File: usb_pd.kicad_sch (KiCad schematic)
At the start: 81 parts, among them Q1 Q_NMOS_DGS, Q2 Q_NMOS_DGS, Q3 Q_NMOS_DGS, Q4 Q_NMOS_DGS, U5 TPS5403DR, U6 MP28167GQ-P, U7 BQ25731

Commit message: added nfc antenna components, added most of footprints
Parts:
- C14, C30: footprint Capacitor_SMD:C_0805_2012Metric_Pad1.18x1.45mm_HandSolder -> (none)
- C15, C25, C27, C28, C29, C31, C32, C33, C34, C35, C36, C37, C38, C39, C40, C49, C50, C57, C58, C59, C60, C61, C62: footprint (none) -> Capacitor_SMD:C_0603_1608Metric_Pad1.08x0.95mm_HandSolder
- L1: footprint smarthome:Inductor_104CDMCC -> airsoft_controller:Inductor_104CDMCC
- R11, R12, R13, R14, R15, R16, R17, R18, R19, R20, R22, R23, R24, R5, R7, R8, R9: footprint (none) -> Resistor_SMD:R_0603_1608Metric_Pad0.98x0.95mm_HandSolder
- U6: footprint (none) -> airsoft_controller:QFN-16

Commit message: schematic creation
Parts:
- removed Q1, Q2, Q3, Q4: Q_NMOS_DGS, symbol Device:Q_NMOS_DGS
- added C57, C60: 10uF MLCC 25V, Capacitor_SMD:C_0805_2012Metric_Pad1.18x1.45mm_HandSolder, symbol Device:C
- added Q1, Q2: Q_Dual_NMOS, airsoft_controller:Q_DUAL_NMOS_DMT3006LPB, symbol airsoft_controller:Q_Dual_NMOS_G1D1D1D1S2S2S2G2S1
- C14, C44, C45: footprint (none) -> Capacitor_SMD:C_0805_2012Metric_Pad1.18x1.45mm_HandSolder
- C16: renamed from C17; footprint (none) -> Capacitor_SMD:CP_Elec_6.3x5.4; symbol Device:C -> Device:C_Polarized
- C18, C19, C20, C21, C22, C23, C51, C52, C53, C54, C55, C56: value 10uF -> 10uF MLCC 25V; footprint (none) -> Capacitor_SMD:C_0805_2012Metric_Pad1.18x1.45mm_HandSolder
- C30: footprint (none) -> Capacitor_SMD:C_1206_3216Metric_Pad1.33x1.80mm_HandSolder
- C41, C43: footprint (none) -> Capacitor_SMD:CP_Elec_6.3x7.7; symbol Device:C -> Device:C_Polarized
- C42: footprint (none) -> Capacitor_SMD:CP_Elec_5x5.3; symbol Device:C -> Device:C_Polarized
- C46, C47: value 33uF -> 22uF POSCAP 25V; footprint (none) -> Capacitor_SMD:C_1210_3225Metric_Pad1.33x2.70mm_HandSolder; symbol Device:C -> Device:C_Polarized
- C48: value 10uF -> 10uF MLCC 25V; footprint (none) -> Capacitor_SMD:C_1206_3216Metric_Pad1.33x1.80mm_HandSolder
- L2: footprint (none) -> airsoft_controller:Inductor_SRP1265C
- L3: footprint (none) -> airsoft_controller:Inductor_WLPMA0A040
- R21: footprint (none) -> Resistor_SMD:R_0612_1632Metric_Pad1.18x3.40mm_HandSolder
- R8: renamed from R10; footprint (none) -> Resistor_SMD:R_0612_1632Metric_Pad1.18x3.40mm_HandSolder
- renumbered C16 to C17, C29 to C28, C28 to C29, C57 to C63, C60 to C64, R12 to R10, R13 to R11, R14 to R12, R15 to R13, R16 to R14, R17 to R15, R18 to R16, R19 to R17, R22 to R18, R23 to R19, R5 to R2, R24 to R22, R4 to R3, R6 to R4, R7 to R5, R8 to R6, R9 to R7, R11 to R9
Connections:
- net BQ_VSYS: now also C46.1, C47.1, C57.2, C60.2, Q2.2 (D1), Q2.3 (D1), Q2.4 (D1); no longer C46.2, C47.2
- net GND: now also C16.2, C25.2, C46.2, C47.2, C57.1, C60.1, Q1.5 (S2), Q1.6 (S2), Q1.7 (S2), Q2.5 (S2), Q2.6 (S2), Q2.7 (S2); no longer C16.1, C25.1, C46.1, C47.1
- net SYS VBUS: now also C16.1; no longer C16.2
- net at C31.2, C32.2, R8.2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: now also Q1.2 (D1), Q1.3 (D1), Q1.4 (D1)
- net at C35.2, L2.1, U7.32 (SW1): now also Q1.9 (S1/D2), Q1.9 (S1/D2)
- net at C40.2, L2.2, U7.23 (SW2): now also Q2.9 (S1/D2), Q2.9 (S1/D2)
- net at C27.1, R6.2, U7.3 (ACP): now also C25.1; no longer C25.2
- net at U7.31 (HIDRV1): now also Q1.1 (G1)
- net at U7.29 (LODRV1): now also Q1.8 (G2)
- net at U7.26 (LODRV2): now also Q2.8 (G2)
- net at U7.24 (HIDRV2): now also Q2.1 (G1)
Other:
- note added: "10nF - 400kHz open - 800kHz"
- note added: "65W - 7*10uF >90W - 9*10uF"
- note added: "Optional"
- moved on the sheet: C14, C15, C25, C27, C29, C63, C64, R2, R20, R21, R22

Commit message: edited usb pcb part
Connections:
- net +3V3 is gone; now on net +3.3V: R15.1
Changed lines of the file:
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@@
     (pin "2")
   )
-  (symbol (lib_id "power:+3V3") (at 180.34 113.03 0) (unit 1)
+  (symbol (lib_id "power:+3.3V") (at 180.34 113.03 0) (unit 1)
     (in_bom yes) (on_board yes) (fields_autoplaced)
     (property "Reference" "#PWR065" (id 0) (at 180.34 116.84 0)

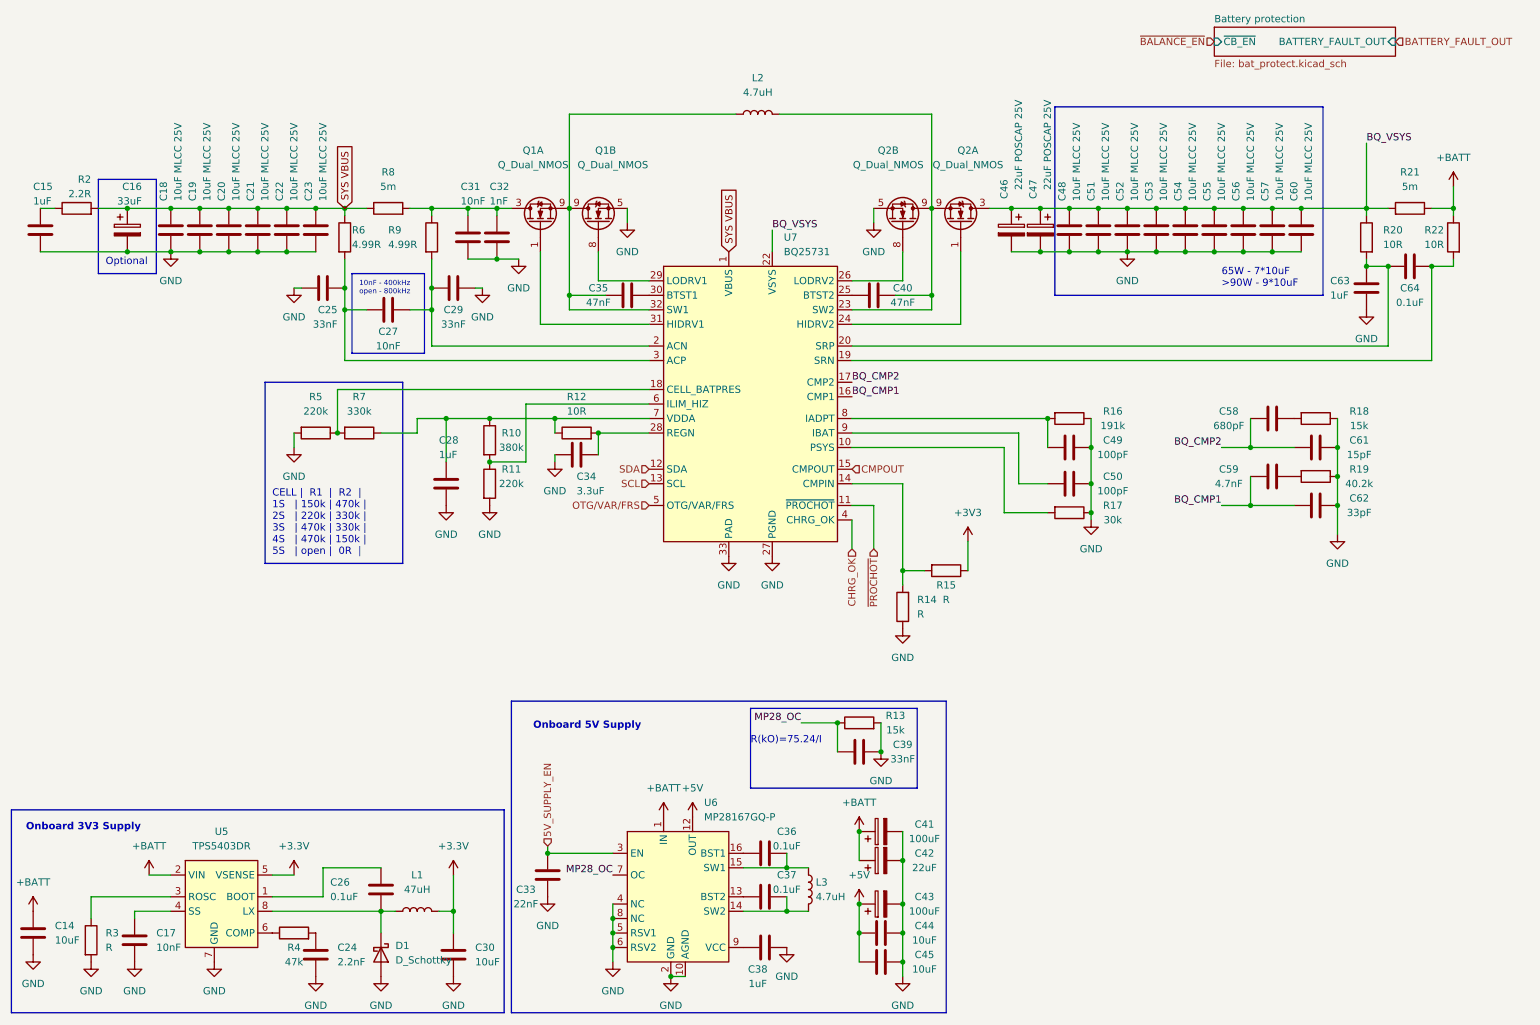
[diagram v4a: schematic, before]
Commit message: done first iteration of pcb routing, slikscreen still broken
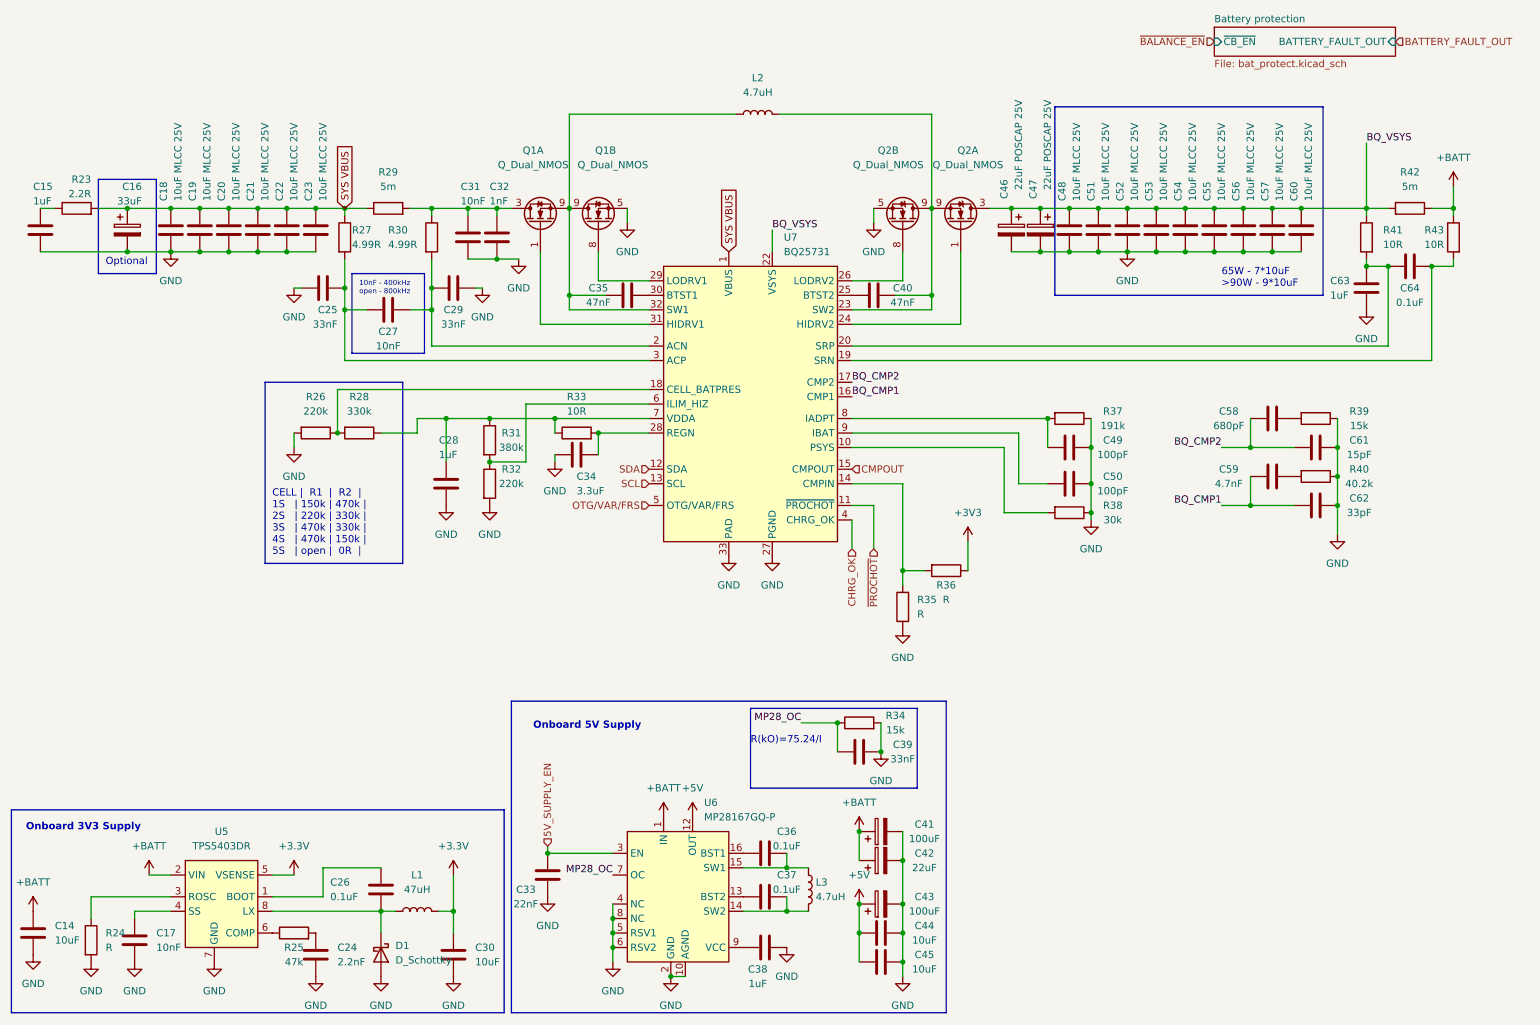
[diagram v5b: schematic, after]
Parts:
- C30, C48: footprint Capacitor_SMD:C_1206_3216Metric_Pad1.33x1.80mm_HandSolder -> Capacitor_SMD:C_0805_2012Metric_Pad1.18x1.45mm_HandSolder
- renumbered R2 to R23, R3 to R24, R4 to R25, R5 to R26, R6 to R27, R7 to R28, R8 to R29, R9 to R30, R10 to R31, R11 to R32, R12 to R33, R13 to R34, R14 to R35, R15 to R36, R16 to R37, R17 to R38, R18 to R39, R19 to R40, R20 to R41, R21 to R42, R22 to R43

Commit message: mounting holes, fixes silkscreen
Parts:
- renumbered R23 to R22, R24 to R23, R25 to R24, R26 to R25, R27 to R26, R28 to R27, R29 to R28, R30 to R29, R31 to R30, R32 to R31, R33 to R32, R34 to R33, R35 to R34, R36 to R35, R37 to R36, R38 to R37, R39 to R38, R40 to R39, R41 to R40, R42 to R41, R43 to R42
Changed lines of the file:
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@@
   (symbol (lib_id "Device:R") (at 86.36 59.69 0) (unit 1)
     (in_bom yes) (on_board yes)
-    (property "Reference" "R30" (id 0) (at 78.74 58.42 0)
+    (property "Reference" "R29" (id 0) (at 78.74 58.42 0)
       (effects (font (size 1.27 1.27)) (justify left))
     )
@@
   (symbol (lib_id "Device:R") (at 96.52 102.87 0) (unit 1)
     (in_bom yes) (on_board yes)
-    (property "Reference" "R32" (id 0) (at 100.33 100.33 0))
+    (property "Reference" "R31" (id 0) (at 100.33 100.33 0))
     (property "Value" "220k" (id 1) (at 100.33 102.87 0))
     (property "Footprint" "Resistor_SMD:R_0603_1608Metric_Pad0.98x0.95mm_HandSolder" (id 2) (at 94.742 102.87 90)
@@
   (symbol (lib_id "Device:R") (at 71.12 59.69 0) (unit 1)
     (in_bom yes) (on_board yes)
-    (property "Reference" "R27" (id 0) (at 72.39 58.42 0)
+    (property "Reference" "R26" (id 0) (at 72.39 58.42 0)
       (effects (font (size 1.27 1.27)) (justify left))
     )
@@
   (symbol (lib_id "Device:R") (at 176.53 118.11 270) (unit 1)
     (in_bom yes) (on_board yes)
-    (property "Reference" "R36" (id 0) (at 176.53 120.65 90))
+    (property "Reference" "R35" (id 0) (at 176.53 120.65 90))
     (property "Value" "R" (id 1) (at 176.53 123.19 90))
     (property "Footprint" "Resistor_SMD:R_0603_1608Metric_Pad0.98x0.95mm_HandSolder" (id 2) (at 176.53 116.332 90)
@@
   (symbol (lib_id "Device:R") (at 265.43 59.69 0) (mirror y) (unit 1)
     (in_bom yes) (on_board yes)
-    (property "Reference" "R43" (id 0) (at 260.35 58.42 0)
+    (property "Reference" "R42" (id 0) (at 260.35 58.42 0)
       (effects (font (size 1.27 1.27)) (justify right))
     )
@@
   (symbol (lib_id "Device:R") (at 78.74 54.61 90) (unit 1)
     (in_bom yes) (on_board yes) (fields_autoplaced)
-    (property "Reference" "R29" (id 0) (at 78.74 48.26 90))
+    (property "Reference" "R28" (id 0) (at 78.74 48.26 90))
     (property "Value" "5m" (id 1) (at 78.74 50.8 90))
     (property "Footprint" "Resistor_SMD:R_0612_1632Metric_Pad1.18x3.40mm_HandSolder" (id 2) (at 78.74 56.388 90)
@@
   (symbol (lib_id "Device:R") (at 62.23 181.61 90) (unit 1)
     (in_bom yes) (on_board yes)
-    (property "Reference" "R25" (id 0) (at 62.23 184.15 90))
+    (property "Reference" "R24" (id 0) (at 62.23 184.15 90))
     (property "Value" "47k" (id 1) (at 62.23 186.69 90))
     (property "Footprint" "Resistor_SMD:R_0603_1608Metric_Pad0.98x0.95mm_HandSolder" (id 2) (at 62.23 183.388 90)
@@
   (symbol (lib_id "Device:R") (at 168.91 124.46 180) (unit 1)
     (in_bom yes) (on_board yes) (fields_autoplaced)
-    (property "Reference" "R35" (id 0) (at 171.45 123.1899 0)
+    (property "Reference" "R34" (id 0) (at 171.45 123.1899 0)
       (effects (font (size 1.27 1.27)) (justify right))
     )
@@
   (symbol (lib_id "Device:R") (at 24.13 54.61 90) (unit 1)
     (in_bom yes) (on_board yes)
-    (property "Reference" "R23" (id 0) (at 26.67 49.53 90)
+    (property "Reference" "R22" (id 0) (at 26.67 49.53 90)
       (effects (font (size 1.27 1.27)) (justify left))
     )
@@
   (symbol (lib_id "Device:R") (at 250.19 59.69 0) (mirror y) (unit 1)
     (in_bom yes) (on_board yes)
-    (property "Reference" "R41" (id 0) (at 256.54 58.42 0)
+    (property "Reference" "R40" (id 0) (at 256.54 58.42 0)
       (effects (font (size 1.27 1.27)) (justify left))
     )
@@
   (symbol (lib_id "Device:R") (at 111.76 93.98 90) (unit 1)
     (in_bom yes) (on_board yes) (fields_autoplaced)
-    (property "Reference" "R33" (id 0) (at 111.76 87.63 90))
+    (property "Reference" "R32" (id 0) (at 111.76 87.63 90))
     (property "Value" "10R" (id 1) (at 111.76 90.17 90))
     (property "Footprint" "Resistor_SMD:R_0603_1608Metric_Pad0.98x0.95mm_HandSolder" (id 2) (at 111.76 95.758 90)
@@
   (symbol (lib_id "Device:R") (at 73.66 93.98 270) (unit 1)
     (in_bom yes) (on_board yes) (fields_autoplaced)
-    (property "Reference" "R28" (id 0) (at 73.66 87.63 90))
+    (property "Reference" "R27" (id 0) (at 73.66 87.63 90))
     (property "Value" "330k" (id 1) (at 73.66 90.17 90))
     (property "Footprint" "Resistor_SMD:R_0603_1608Metric_Pad0.98x0.95mm_HandSolder" (id 2) (at 73.66 92.202 90)
@@
   (symbol (lib_id "Device:R") (at 198.12 107.95 270) (unit 1)
     (in_bom yes) (on_board yes)
-    (property "Reference" "R38" (id 0) (at 205.74 106.68 90))
+    (property "Reference" "R37" (id 0) (at 205.74 106.68 90))
     (property "Value" "30k" (id 1) (at 205.74 109.22 90))
     (property "Footprint" "Resistor_SMD:R_0603_1608Metric_Pad0.98x0.95mm_HandSolder" (id 2) (at 198.12 106.172 90)
@@
   (symbol (lib_id "Device:R") (at 161.29 144.78 90) (unit 1)
     (in_bom yes) (on_board yes)
-    (property "Reference" "R34" (id 0) (at 167.64 143.51 90))
+    (property "Reference" "R33" (id 0) (at 167.64 143.51 90))
     (property "Value" "15k" (id 1) (at 167.64 146.05 90))
     (property "Footprint" "Resistor_SMD:R_0603_1608Metric_Pad0.98x0.95mm_HandSolder" (id 2) (at 161.29 146.558 90)
@@
   (symbol (lib_id "Device:R") (at 257.81 54.61 270) (mirror x) (unit 1)
     (in_bom yes) (on_board yes) (fields_autoplaced)
-    (property "Reference" "R42" (id 0) (at 257.81 48.26 90))
+    (property "Reference" "R41" (id 0) (at 257.81 48.26 90))
     (property "Value" "5m" (id 1) (at 257.81 50.8 90))
     (property "Footprint" "Resistor_SMD:R_0612_1632Metric_Pad1.18x3.40mm_HandSolder" (id 2) (at 257.81 56.388 90)
@@
   (symbol (lib_id "Device:R") (at 26.67 182.88 0) (unit 1)
     (in_bom yes) (on_board yes) (fields_autoplaced)
-    (property "Reference" "R24" (id 0) (at 29.21 181.6099 0)
+    (property "Reference" "R23" (id 0) (at 29.21 181.6099 0)
       (effects (font (size 1.27 1.27)) (justify left))
     )
@@
   (symbol (lib_id "Device:R") (at 241.3 101.6 270) (unit 1)
     (in_bom yes) (on_board yes)
-    (property "Reference" "R40" (id 0) (at 248.92 100.33 90))
+    (property "Reference" "R39" (id 0) (at 248.92 100.33 90))
     (property "Value" "40.2k" (id 1) (at 248.92 102.87 90))
     (property "Footprint" "Resistor_SMD:R_0603_1608Metric_Pad0.98x0.95mm_HandSolder" (id 2) (at 241.3 99.822 90)
@@
   (symbol (lib_id "Device:R") (at 241.3 91.44 270) (unit 1)
     (in_bom yes) (on_board yes)
-    (property "Reference" "R39" (id 0) (at 248.92 90.17 90))
+    (property "Reference" "R38" (id 0) (at 248.92 90.17 90))
     (property "Value" "15k" (id 1) (at 248.92 92.71 90))
     (property "Footprint" "Resistor_SMD:R_0603_1608Metric_Pad0.98x0.95mm_HandSolder" (id 2) (at 241.3 89.662 90)
@@
   (symbol (lib_id "Device:R") (at 66.04 93.98 270) (unit 1)
     (in_bom yes) (on_board yes) (fields_autoplaced)
-    (property "Reference" "R26" (id 0) (at 66.04 87.63 90))
+    (property "Reference" "R25" (id 0) (at 66.04 87.63 90))
     (property "Value" "220k" (id 1) (at 66.04 90.17 90))
     (property "Footprint" "Resistor_SMD:R_0603_1608Metric_Pad0.98x0.95mm_HandSolder" (id 2) (at 66.04 92.202 90)
@@
   (symbol (lib_id "Device:R") (at 198.12 91.44 270) (unit 1)
     (in_bom yes) (on_board yes)
-    (property "Reference" "R37" (id 0) (at 205.74 90.17 90))
+    (property "Reference" "R36" (id 0) (at 205.74 90.17 90))
     (property "Value" "191k" (id 1) (at 205.74 92.71 90))
     (property "Footprint" "Resistor_SMD:R_0603_1608Metric_Pad0.98x0.95mm_HandSolder" (id 2) (at 198.12 89.662 90)
@@
   (symbol (lib_id "Device:R") (at 96.52 95.25 0) (unit 1)
     (in_bom yes) (on_board yes)
-    (property "Reference" "R31" (id 0) (at 100.33 93.98 0))
+    (property "Reference" "R30" (id 0) (at 100.33 93.98 0))
     (property "Value" "380k" (id 1) (at 100.33 96.52 0))
     (property "Footprint" "Resistor_SMD:R_0603_1608Metric_Pad0.98x0.95mm_HandSolder" (id 2) (at 94.742 95.25 90)

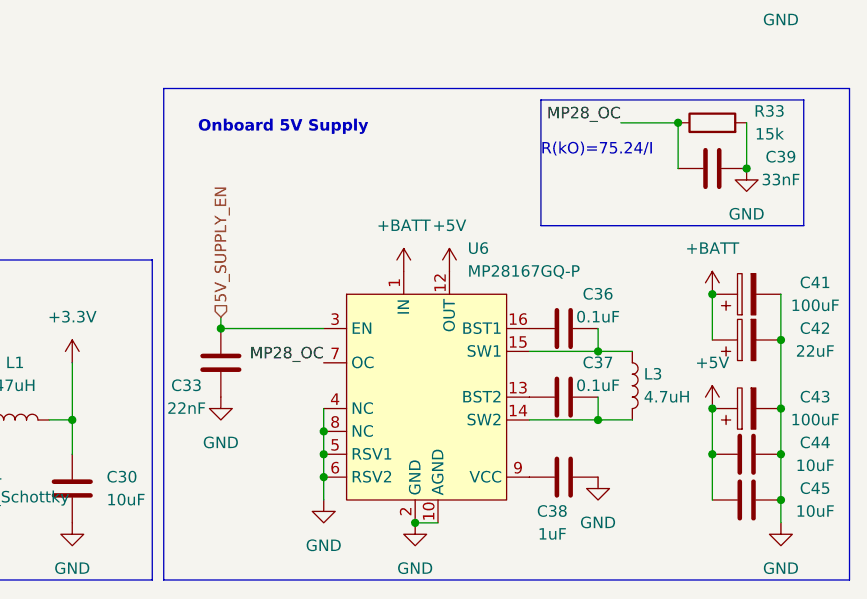
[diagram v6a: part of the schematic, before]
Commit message: copied own LED footprint, modified silkscreen, minor visual changes in schematics
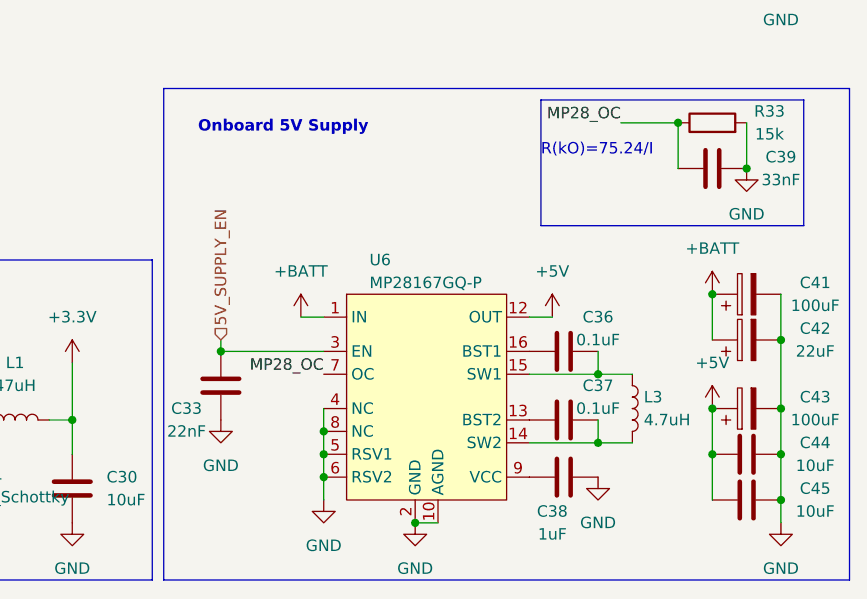
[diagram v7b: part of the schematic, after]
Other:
- moved on the sheet: C33, C36, C37, L3, U6
